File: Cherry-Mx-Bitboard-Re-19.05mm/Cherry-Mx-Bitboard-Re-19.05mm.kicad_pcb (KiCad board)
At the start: 2 copper layers, 18 x 18 mm, 17 parts, among them SW1 SW_Push, SW2 SW_Push-Switch

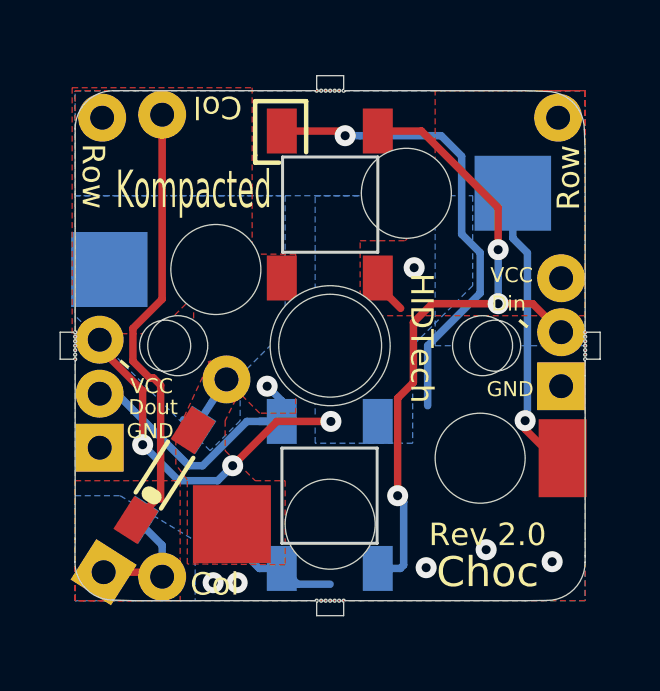
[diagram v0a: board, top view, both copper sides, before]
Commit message: add plaque
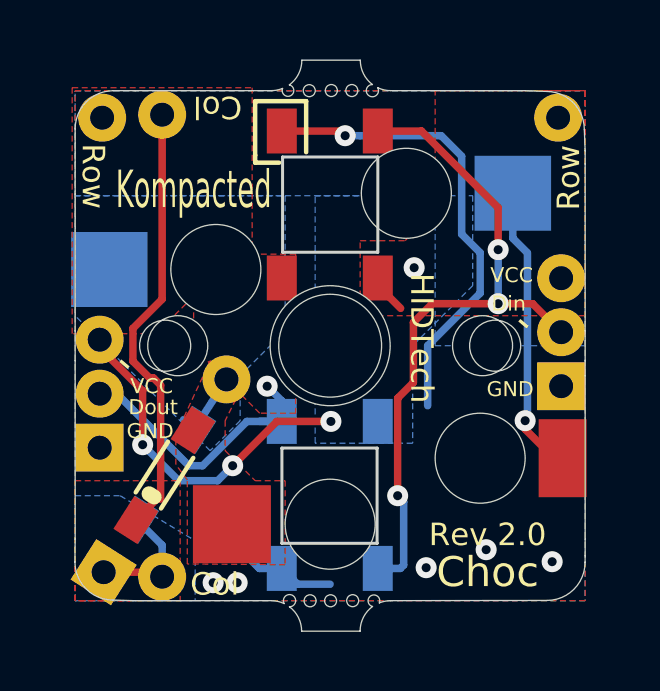
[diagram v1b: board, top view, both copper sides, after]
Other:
- board size 18 x 18 mm -> 17 x 19 mm
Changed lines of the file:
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@@
   (general
     (thickness 1.6)
-    (drawings 114)
+    (drawings 94)
     (tracks 109)
     (zones 0)
@@
     (0 F.Cu signal)
     (31 B.Cu signal)
-    (32 B.Adhes user)
-    (33 F.Adhes user)
-    (34 B.Paste user)
-    (35 F.Paste user)
-    (36 B.SilkS user)
-    (37 F.SilkS user)
+    (32 B.Adhes user hide)
+    (33 F.Adhes user hide)
+    (34 B.Paste user hide)
+    (35 F.Paste user hide)
+    (36 B.SilkS user hide)
+    (37 F.SilkS user hide)
     (38 B.Mask user)
     (39 F.Mask user)
-    (40 Dwgs.User user)
-    (41 Cmts.User user)
-    (42 Eco1.User user)
+    (40 Dwgs.User user hide)
+    (41 Cmts.User user hide)
+    (42 Eco1.User user hide)
     (43 Eco2.User user)
     (44 Edge.Cuts user)
-    (45 Margin user)
-    (46 B.CrtYd user)
-    (47 F.CrtYd user)
-    (48 B.Fab user)
-    (49 F.Fab user)
+    (45 Margin user hide)
+    (46 B.CrtYd user hide)
+    (47 F.CrtYd user hide)
+    (48 B.Fab user hide)
+    (49 F.Fab user hide)
   )
   (setup
@@
     (aux_axis_origin 80.645 139.065)
     (grid_origin 80.645 43.815)
-    (visible_elements 7FFFFF7F)
+    (visible_elements 7EFBB61F)
     (pcbplotparams
       (layerselection 0x010fc_ffffffff)
@@
       (net 3 Row1))
   )
+  (gr_line (start 86.144999 62.315) (end 90.678 62.31382) (layer Edge.Cuts) (width 0.01))
+  (gr_line (start 94.6658 62.31382) (end 99.8728 62.3062) (layer Edge.Cuts) (width 0.01))
+  (gr_line (start 101.145 53.315) (end 101.145 54.315) (layer Edge.Cuts) (width 0.01))
+  (gr_arc (start 91.2908 62.31382) (end 91.112196 62.411272) (angle 299.3116114) (layer Edge.Cuts) (width 0.01))
+  (gr_arc (start 94.1038 62.31782) (end 94.284799 62.390019) (angle -278.3) (layer Edge.Cuts) (width 0.01))
+  (gr_arc (start 94.6658 63.32982) (end 94.6658 62.31382) (angle -22.10000965) (layer Edge.Cuts) (width 0.01))
+  (gr_arc (start 94.6658 63.32982) (end 94.058512 62.507353) (angle -53.6) (layer Edge.Cuts) (width 0.01))
+  (gr_arc (start 90.678 63.32982) (end 90.678 62.31382) (angle 25.30001782) (layer Edge.Cuts) (width 0.01))
+  (gr_arc (start 90.678 63.32982) (end 91.288338 62.517266) (angle 53.13714983) (layer Edge.Cuts) (width 0.01))
+  (gr_line (start 93.643425 63.330555) (end 91.694246 63.330683) (layer Edge.Cuts) (width 0.01))
+  (gr_circle (center 91.9766 62.31782) (end 91.7766 62.31782) (layer Edge.Cuts) (width 0.01))
+  (gr_circle (center 92.6592 62.31782) (end 92.4592 62.31782) (layer Edge.Cuts) (width 0.01))
+  (gr_circle (center 93.3958 62.31382) (end 93.1958 62.31382) (layer Edge.Cuts) (width 0.01))
+  (gr_line (start 84.1375 61.0235) (end 84.145 60.265) (layer Edge.Cuts) (width 0.01))
+  (gr_line (start 101.145 54.315) (end 101.145 54.815) (layer Edge.Cuts) (width 0.01))
+  (gr_line (start 84.145 53.315) (end 84.145 54.315) (layer Edge.Cuts) (width 0.01))
+  (gr_arc (start 94.6658 44.2976) (end 94.055462 45.110154) (angle 53.13714983) (layer Edge.Cuts) (width 0.01))
+  (gr_arc (start 94.6658 44.2976) (end 94.6658 45.3136) (angle 25.30001782) (layer Edge.Cuts) (width 0.01))
+  (gr_arc (start 94.053 45.3136) (end 94.231604 45.216148) (angle 299.3116114) (layer Edge.Cuts) (width 0.01))
+  (gr_arc (start 90.678 44.2976) (end 90.678 45.3136) (angle -22.10000965) (layer Edge.Cuts) (width 0.01))
+  (gr_arc (start 90.678 44.2976) (end 91.284913 45.121754) (angle -53.67299974) (layer Edge.Cuts) (width 0.01))
+  (gr_arc (start 91.24 45.3096) (end 91.060244 45.238953) (angle -278.008942) (layer Edge.Cuts) (width 0.01))
+  (gr_line (start 99.145001 45.314999) (end 97.773401 45.314999) (layer Edge.Cuts) (width 0.01))
+  (gr_line (start 91.70151 44.296864) (end 93.649554 44.296737) (layer Edge.Cuts) (width 0.01))
+  (gr_circle (center 93.3672 45.3096) (end 93.5672 45.3096) (layer Edge.Cuts) (width 0.01))
+  (gr_circle (center 92.6846 45.3096) (end 92.8846 45.3096) (layer Edge.Cuts) (width 0.01))
+  (gr_circle (center 91.948 45.3136) (end 92.148 45.3136) (layer Edge.Cuts) (width 0.01))
   (gr_line (start 84.145 53.315) (end 84.145 48.765) (layer Edge.Cuts) (width 0.01))
-  (gr_circle (center 84.145 53.515) (end 84.095 53.515) (layer Edge.Cuts) (width 0.01))
-  (gr_circle (center 84.145 53.815) (end 84.095 53.815) (layer Edge.Cuts) (width 0.01))
-  (gr_line (start 83.645 53.365) (end 84.095 53.365) (layer Edge.Cuts) (width 0.01))
-  (gr_arc (start 84.145 53.365) (end 84.145 53.315) (angle 270) (layer Edge.Cuts) (width 0.01))
-  (gr_line (start 84.095 54.265) (end 83.645 54.265) (layer Edge.Cuts) (width 0.01))
-  (gr_circle (center 84.145 53.665) (end 84.095 53.665) (layer Edge.Cuts) (width 0.01))
-  (gr_circle (center 84.145 53.965) (end 84.095 53.965) (layer Edge.Cuts) (width 0.01))
-  (gr_arc (start 84.145 54.265) (end 84.095 54.265) (angle 270) (layer Edge.Cuts) (width 0.01))
-  (gr_circle (center 84.145 54.115) (end 84.095 54.115) (layer Edge.Cuts) (width 0.01))
-  (gr_line (start 83.645 54.265) (end 83.645 53.365) (layer Edge.Cuts) (width 0.01))
-  (gr_circle (center 101.145 53.515) (end 101.195 53.515) (layer Edge.Cuts) (width 0.01))
-  (gr_circle (center 101.145 53.815) (end 101.195 53.815) (layer Edge.Cuts) (width 0.01))
-  (gr_line (start 101.645 53.365) (end 101.195 53.365) (layer Edge.Cuts) (width 0.01))
-  (gr_arc (start 101.145 53.365) (end 101.145 53.315) (angle -270) (layer Edge.Cuts) (width 0.01))
-  (gr_line (start 101.195 54.265) (end 101.645 54.265) (layer Edge.Cuts) (width 0.01))
-  (gr_circle (center 101.145 53.665) (end 101.195 53.665) (layer Edge.Cuts) (width 0.01))
-  (gr_circle (center 101.145 53.965) (end 101.195 53.965) (layer Edge.Cuts) (width 0.01))
-  (gr_arc (start 101.145 54.265) (end 101.195 54.265) (angle -270) (layer Edge.Cuts) (width 0.01))
-  (gr_circle (center 101.145 54.115) (end 101.195 54.115) (layer Edge.Cuts) (width 0.01))
-  (gr_line (start 101.645 54.265) (end 101.645 53.365) (layer Edge.Cuts) (width 0.01))
-  (gr_line (start 92.145 62.315) (end 91.869998 62.314999) (layer Edge.Cuts) (width 0.01))
-  (gr_line (start 93.67 62.315001) (end 93.145 62.315) (layer Edge.Cuts) (width 0.01))
-  (gr_circle (center 92.945 62.315) (end 92.945 62.365) (layer Edge.Cuts) (width 0.01))
-  (gr_circle (center 92.645 62.315) (end 92.645 62.365) (layer Edge.Cuts) (width 0.01))
-  (gr_line (start 93.095 62.815) (end 93.095 62.365) (layer Edge.Cuts) (width 0.01))
-  (gr_arc (start 93.095 62.315) (end 93.145 62.315) (angle -270) (layer Edge.Cuts) (width 0.01))
-  (gr_line (start 92.195 62.365) (end 92.195 62.815) (layer Edge.Cuts) (width 0.01))
-  (gr_circle (center 92.795 62.315) (end 92.795 62.365) (layer Edge.Cuts) (width 0.01))
-  (gr_circle (center 92.495 62.315) (end 92.495 62.365) (layer Edge.Cuts) (width 0.01))
-  (gr_arc (start 92.195 62.315) (end 92.195 62.365) (angle -270) (layer Edge.Cuts) (width 0.01))
-  (gr_circle (center 92.345 62.315) (end 92.345 62.365) (layer Edge.Cuts) (width 0.01))
-  (gr_line (start 92.195 62.815) (end 93.095 62.815) (layer Edge.Cuts) (width 0.01))
-  (gr_line (start 93.145 45.315) (end 99.145001 45.314999) (layer Edge.Cuts) (width 0.01))
-  (gr_line (start 92.145 45.315) (end 86.145 45.315001) (layer Edge.Cuts) (width 0.01))
-  (gr_circle (center 92.345 45.315) (end 92.345 45.265) (layer Edge.Cuts) (width 0.01))
-  (gr_circle (center 92.645 45.315) (end 92.645 45.265) (layer Edge.Cuts) (width 0.01))
-  (gr_line (start 92.195 44.815) (end 92.195 45.265) (layer Edge.Cuts) (width 0.01))
-  (gr_arc (start 92.195 45.315) (end 92.145 45.315) (angle -270) (layer Edge.Cuts) (width 0.01))
-  (gr_line (start 93.095 45.265) (end 93.095 44.815) (layer Edge.Cuts) (width 0.01))
-  (gr_circle (center 92.495 45.315) (end 92.495 45.265) (layer Edge.Cuts) (width 0.01))
-  (gr_circle (center 92.795 45.315) (end 92.795 45.265) (layer Edge.Cuts) (width 0.01))
-  (gr_arc (start 93.095 45.315) (end 93.095 45.265) (angle -270) (layer Edge.Cuts) (width 0.01))
-  (gr_circle (center 92.945 45.315) (end 92.945 45.265) (layer Edge.Cuts) (width 0.01))
-  (gr_line (start 93.095 44.815) (end 92.195 44.815) (layer Edge.Cuts) (width 0.01))
+  (gr_line (start 94.6658 45.3136) (end 97.773401 45.314999) (layer Edge.Cuts) (width 0.01))
+  (gr_line (start 90.678 45.3136) (end 86.145 45.315001) (layer Edge.Cuts) (width 0.01))
   (gr_line (start 101.145 47.765) (end 101.145 47.314999) (layer Edge.Cuts) (width 0.01))
   (gr_line (start 101.145 60.815) (end 101.145 60.265) (layer Edge.Cuts) (width 0.01))
@@
     (effects (font (size 0.75 0.75) (thickness 0.15)) (justify mirror))
   )
-  (gr_line (start 101.145 54.315) (end 101.145 54.815) (layer Edge.Cuts) (width 0.01))
   (gr_text Col (at 88.845 61.765) (layer B.SilkS)
     (effects (font (size 0.75 0.75) (thickness 0.1875)) (justify mirror))
@@
   )
   (gr_line (start 94.234 50.7) (end 94.234 47.525) (layer Edge.Cuts) (width 0.1))
-  (gr_line (start 84.1375 61.0235) (end 84.145 60.265) (layer Edge.Cuts) (width 0.01))
   (gr_line (start 91.059 47.525) (end 91.059 50.7) (layer Edge.Cuts) (width 0.1))
   (gr_line (start 94.234 47.525) (end 91.059 47.525) (layer Edge.Cuts) (width 0.1))
@@
   (gr_line (start 99.145001 45.314999) (end 99.8474 45.339) (layer Edge.Cuts) (width 0.01))
   (gr_arc (start 99.8474 46.609) (end 101.1174 46.609) (angle -90) (layer Edge.Cuts) (width 0.01))
-  (gr_line (start 99.8728 62.3062) (end 99.145001 62.315) (layer Edge.Cuts) (width 0.01))
   (gr_arc (start 99.8728 61.0362) (end 99.8728 62.3062) (angle -90) (layer Edge.Cuts) (width 0.01))
   (gr_line (start 86.144999 62.315) (end 85.4075 62.2935) (layer Edge.Cuts) (width 0.01))
@@
     (effects (font (size 0.75 0.75) (thickness 0.15)))
   )
-  (gr_line (start 93.67 62.315001) (end 99.145001 62.315) (layer Edge.Cuts) (width 0.01))
   (gr_line (start 101.145 54.815) (end 101.145 60.265) (layer Edge.Cuts) (width 0.01))
-  (gr_line (start 86.144999 62.315) (end 91.869998 62.314999) (layer Edge.Cuts) (width 0.01))
   (gr_line (start 84.145 54.315) (end 84.145 60.265) (layer Edge.Cuts) (width 0.01))
   (gr_line (start 101.145 47.765) (end 101.145 53.315) (layer Edge.Cuts) (width 0.01))

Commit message: switch to sk6812 mini-e
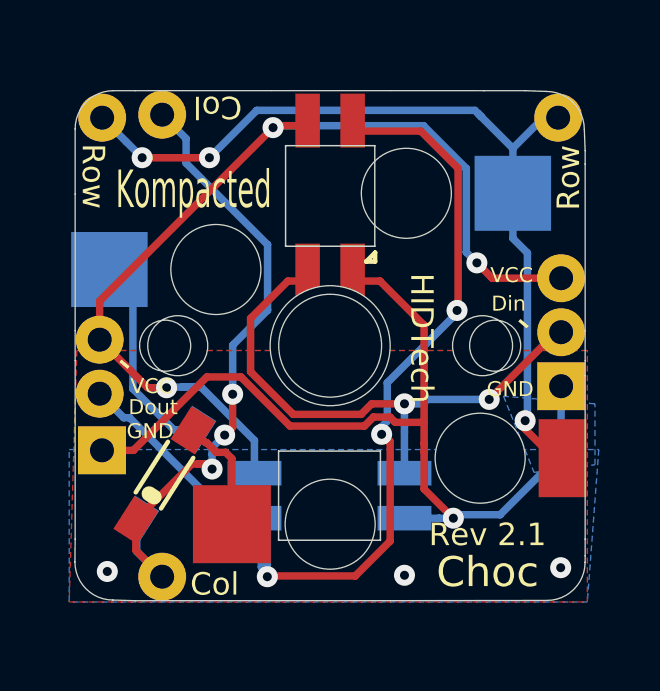
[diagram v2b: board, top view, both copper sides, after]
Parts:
- removed D1: 1N4148W, Footprints:1N4148W
- D5: value SK6812 -> SK6812MINI_E; footprint customs:LED_SK6812_PLCC4_5.0x5.0mm_P3.2mm_FLIP -> customs:YS-SK6812MINI-E_REVERSE; moved to F.Cu
- D6: value SK6812 -> SK6812MINI_E; footprint customs:LED_SK6812_PLCC4_5.0x5.0mm_P3.2mm_FLIP -> customs:YS-SK6812MINI-E_REVERSE; moved to B.Cu
- moved D5 9.98 mm to (92.6, 48.8), turned to 90 degrees
- moved D6 9.71 mm to (92.6, 58.8), turned to 180 degrees
- moved GND1 0.12 mm to (85.0, 57.3)
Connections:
- D5 pad 1: GND -> VCC
- D5 pad 2: Din -> Dout
- D5 pad 3: VCC -> GND
- D5 pad 4: Dout -> Din
- D6 pad 1: GND -> VCC
- D6 pad 2: Din -> Dout
- D6 pad 3: VCC -> GND
- D6 pad 4: Dout -> Din
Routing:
- net Dout: track 10.3 -> 34.4 mm, vias 1 -> 3
- net VCC: track 13.7 -> 33.1 mm, vias 4 -> 3
- net Row1: track 12.0 -> 31.0 mm, vias 1 -> 3
- net GND: track 18.8 -> 30.8 mm, vias 6 -> 4
- net Net-(D1-Pad2): track 7.84 -> 15.3 mm
- net Din: track 23.1 -> 18.6 mm, vias 3 -> 2
- net Col1: track 19.1 -> 22.8 mm, vias 0 -> 3
- removed copper zone on B.Cu, net Col1
- removed copper zone on F.Cu, net Col1
- removed copper zone on F.Cu, net Dout
- removed copper zone on B.Cu, net Net-(D1-Pad2)
- removed copper zone on F.Cu, net Net-(D1-Pad2)
- removed copper zone on B.Cu, net Row1
- removed copper zone on B.Cu, net VCC
- removed copper zone on F.Cu, net VCC
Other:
- board size 17 x 19 mm -> 17 x 17 mm
- net class Default: via_dia 0.4 -> 0.7
- board text added: "Rev 2.1"
- board text removed: "Rev 2.0"
